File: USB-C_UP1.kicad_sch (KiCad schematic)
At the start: 23 parts, among them J12 USB_C_Receptacle, J13 I2C_HD3SS3220, U26 HD3SS3220IRNHR, U27 TPD4E02B04DQA, U28 TPD4E02B04DQA, U29 TPD4E02B04DQA

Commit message: Added lcsc part number for most of resistors
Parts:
- R93, R94: LCSC Part (none) -> C25764
- R95, R96, R97: LCSC Part (none) -> C105871
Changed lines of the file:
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@@
+			)
+		)
+		(property "LCSC Part" "C105871"
+			(at 81.28 168.91 0)
+			(effects
+				(font
+					(size 1.27 1.27)
+				)
+				(hide yes)
 			)
 		)
@@
 			)
 		)
+		(property "LCSC Part" "C105871"
+			(at 73.66 171.45 0)
+			(effects
+				(font
+					(size 1.27 1.27)
+				)
+				(hide yes)
+			)
+		)
 		(pin "2"
 		)
@@
 			)
 		)
+		(property "LCSC Part" "C25764 "
+			(at 34.29 54.61 0)
+			(effects
+				(font
+					(size 1.27 1.27)
+				)
+				(hide yes)
+			)
+		)
 		(pin "1"
 		)
@@
 			)
 		)
+		(property "LCSC Part" "C25764 "
+			(at 41.91 52.07 0)
+			(effects
+				(font
+					(size 1.27 1.27)
+				)
+				(hide yes)
+			)
+		)
 		(pin "1"
 		)
@@
 			(effects
 				(font
+					(size 1.27 1.27)
+				)
+				(hide yes)
+			)
+		)
+		(property "LCSC Part" "C105871"
+			(at 49.53 66.04 90)
+			(effects
+				(font

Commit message: minor schematic fixes, footprints changes, layout improvements
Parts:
- removed TP11: Out1, TestPoint:TestPoint_Loop_D1.80mm_Drill1.0mm_Beaded, symbol Connector:TestPoint
- removed TP12: Out2, TestPoint:TestPoint_Loop_D1.80mm_Drill1.0mm_Beaded, symbol Connector:TestPoint
- C121: footprint Capacitor_THT:C_Radial_D6.3mm_H11.0mm_P2.50mm -> Capacitor_SMD:C_0805_2012Metric; LCSC Part C109392 -> C141660
- TP10, TP9: footprint TestPoint:TestPoint_Loop_D1.80mm_Drill1.0mm_Beaded -> TestPoint:TestPoint_Pad_D1.0mm
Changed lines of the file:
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@@
 	)
 	(junction
-		(at 60.96 175.26)
-		(diameter 0)
-		(color 0 0 0 0)
-	)
-	(junction
-		(at 52.07 172.72)
-		(diameter 0)
-		(color 0 0 0 0)
-	)
-	(junction
 		(at 233.68 40.64)
 		(diameter 0)
@@
 	(wire
 		(pts
-			(xy 60.96 175.26) (xy 73.66 175.26)
-		)
-		(stroke
-			(width 0)
-			(type default)
-		)
-	)
-	(wire
-		(pts
 			(xy 233.68 66.04) (xy 218.44 66.04)
 		)
@@
 	(wire
 		(pts
-			(xy 30.48 175.26) (xy 60.96 175.26)
+			(xy 30.48 175.26) (xy 73.66 175.26)
 		)
 		(stroke
@@
 	(wire
 		(pts
-			(xy 30.48 172.72) (xy 52.07 172.72)
+			(xy 30.48 172.72) (xy 81.28 172.72)
 		)
 		(stroke
@@
 	(wire
 		(pts
-			(xy 52.07 172.72) (xy 81.28 172.72)
-		)
-		(stroke
-			(width 0)
-			(type default)
-		)
-	)
-	(wire
-		(pts
 			(xy 127 76.2) (xy 140.97 76.2)
 		)
@@
 	)
 	(symbol
-		(lib_id "Connector:TestPoint")
-		(at 52.07 172.72 0)
-		(unit 1)
-		(exclude_from_sim no)
-		(in_bom yes)
-		(on_board yes)
-		(dnp no)
-		(fields_autoplaced yes)
-		(property "Reference" "TP11"
-			(at 54.61 168.1479 0)
-			(effects
-				(font
-					(size 1.27 1.27)
-				)
-				(justify left)
-			)
-		)
-		(property "Value" "Out1"
-			(at 54.61 170.6879 0)
-			(effects
-				(font
-					(size 1.27 1.27)
-				)
-				(justify left)
-			)
-		)
-		(property "Footprint" "TestPoint:TestPoint_Loop_D1.80mm_Drill1.0mm_Beaded"
-			(at 57.15 172.72 0)
-			(effects
-				(font
-					(size 1.27 1.27)
-				)
-				(hide yes)
-			)
-		)
-		(property "Datasheet" "~"
-			(at 57.15 172.72 0)
-			(effects
-				(font
-					(size 1.27 1.27)
-				)
-				(hide yes)
-			)
-		)
-		(property "Description" "test point"
-			(at 52.07 172.72 0)
-			(effects
-				(font
-					(size 1.27 1.27)
-				)
-				(hide yes)
-			)
-		)
-		(pin "1"
-		)
-		(instances
-			(project "USB_hub"
-				(path "/a2586c28-95f1-49e6-9254-37d7a8473e53/c482699f-16ee-4a02-bb28-667e2389d2fc"
-					(reference "TP11")
-					(unit 1)
-				)
-			)
-		)
-	)
-	(symbol
 		(lib_id "2025-07-15_13-22-11:HD3SS3220IRNHR")
 		(at 96.52 66.04 0)
@@
 	)
 	(symbol
-		(lib_id "Connector:TestPoint")
-		(at 60.96 175.26 0)
-		(unit 1)
-		(exclude_from_sim no)
-		(in_bom yes)
-		(on_board yes)
-		(dnp no)
-		(property "Reference" "TP12"
-			(at 63.5 171.196 0)
-			(effects
-				(font
-					(size 1.27 1.27)
-				)
-				(justify left)
-			)
-		)
-		(property "Value" "Out2"
-			(at 63.5 173.736 0)
-			(effects
-				(font
-					(size 1.27 1.27)
-				)
-				(justify left)
-			)
-		)
-		(property "Footprint" "TestPoint:TestPoint_Loop_D1.80mm_Drill1.0mm_Beaded"
-			(at 66.04 175.26 0)
-			(effects
-				(font
-					(size 1.27 1.27)
-				)
-				(hide yes)
-			)
-		)
-		(property "Datasheet" "~"
-			(at 66.04 175.26 0)
-			(effects
-				(font
-					(size 1.27 1.27)
-				)
-				(hide yes)
-			)
-		)
-		(property "Description" "test point"
-			(at 60.96 175.26 0)
-			(effects
-				(font
-					(size 1.27 1.27)
-				)
-				(hide yes)
-			)
-		)
-		(pin "1"
-		)
-		(instances
-			(project "USB_hub"
-				(path "/a2586c28-95f1-49e6-9254-37d7a8473e53/c482699f-16ee-4a02-bb28-667e2389d2fc"
-					(reference "TP12")
-					(unit 1)
-				)
-			)
-		)
-	)
-	(symbol
 		(lib_id "power:VBUS")
 		(at 48.26 41.91 0)
@@
 			)
 		)
-		(property "Footprint" "TestPoint:TestPoint_Loop_D1.80mm_Drill1.0mm_Beaded"
+		(property "Footprint" "TestPoint:TestPoint_Pad_D1.0mm"
 			(at 27.94 162.56 0)
 			(effects
@@
 			)
 		)
-		(property "Footprint" "TestPoint:TestPoint_Loop_D1.80mm_Drill1.0mm_Beaded"
+		(property "Footprint" "TestPoint:TestPoint_Pad_D1.0mm"
 			(at 27.94 154.94 0)
 			(effects
@@
 			)
 		)
-		(property "Footprint" "Capacitor_THT:C_Radial_D6.3mm_H11.0mm_P2.50mm"
+		(property "Footprint" "Capacitor_SMD:C_0805_2012Metric"
 			(at 21.2852 34.29 0)
 			(effects
@@
 			)
 		)
-		(property "LCSC Part" "C109392"
+		(property "LCSC Part" "C141660 "
 			(at 20.32 30.48 0)
 			(effects

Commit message: comments to schematic added, changed a few components
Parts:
- R92: footprint Resistor_SMD:R_0402_1005Metric -> Resistor_SMD:R_1206_3216Metric; Mouser Part No  (none) -> 603-RT1206CRE07900KL
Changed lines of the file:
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@@
 			)
 		)
-		(property "Footprint" "Resistor_SMD:R_0402_1005Metric"
+		(property "Footprint" "Resistor_SMD:R_1206_3216Metric"
 			(at 50.038 45.72 90)
 			(effects
@@
 			(at 48.26 45.72 0)
 			(effects
+				(font
+					(size 1.27 1.27)
+				)
+				(hide yes)
+			)
+		)
+		(property "Mouser Part No " "603-RT1206CRE07900KL "
+			(at 48.26 45.72 0)
+			(effects

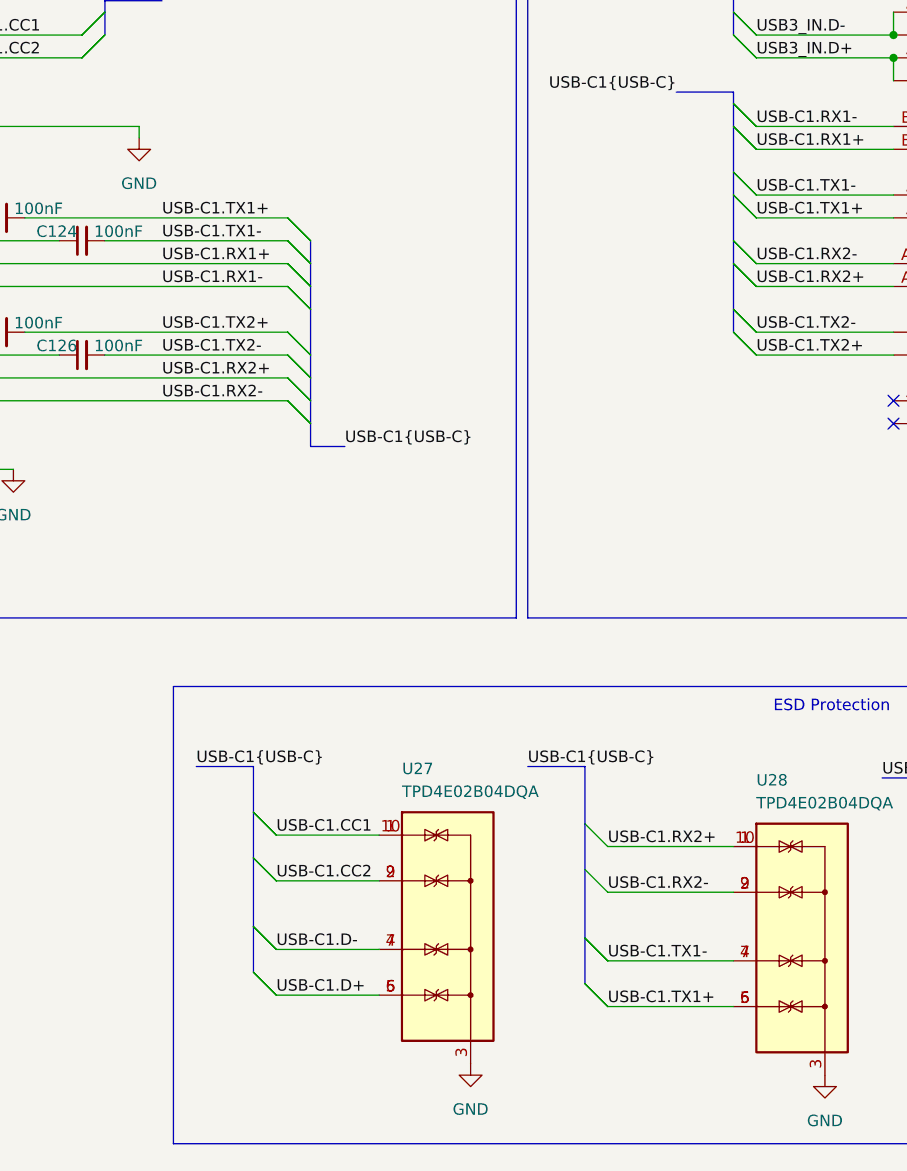
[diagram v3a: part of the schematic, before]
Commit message: Rearrange of the component placement, scheme changes for better routing
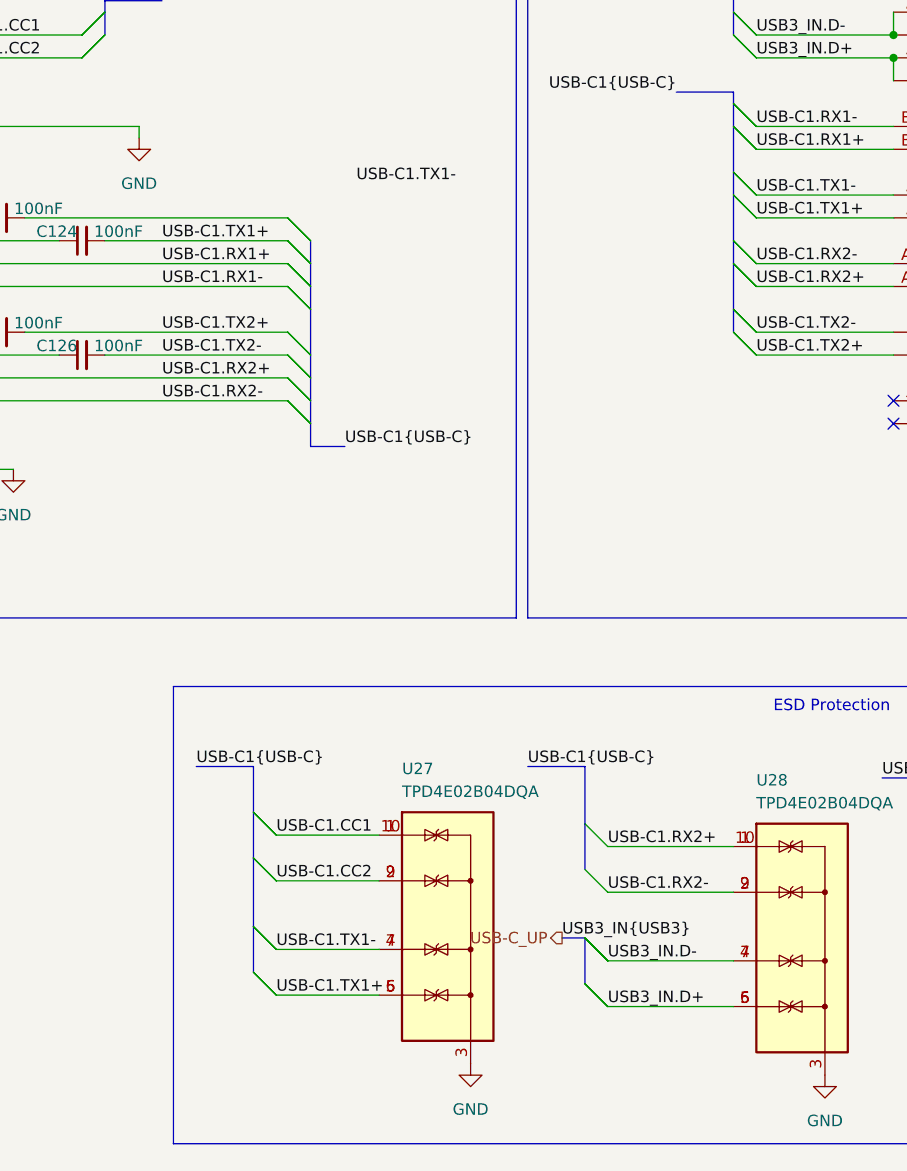
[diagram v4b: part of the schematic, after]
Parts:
- C122, C123, C124, C125, C126: footprint Capacitor_SMD:C_0402_1005Metric -> Capacitor_SMD:C_0201_0603Metric; LCSC Part C5182432 -> C181043
- J13: footprint Connector_PinHeader_1.27mm:PinHeader_1x03_P1.27mm_Vertical -> Connector_PinHeader_1.00mm:PinHeader_1x03_P1.00mm_Vertical
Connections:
- net USB-C1.D+ is gone; now on net USB-C1.TX1+: U27.5 (IO4), U27.6 (NC)
- net USB-C1.D- is gone; now on net USB-C1.TX1-: U27.4 (IO3), U27.7 (NC)
- net USB-C1.TX1+: now also C124.2; no longer C123.2, U28.5 (IO4), U28.6 (NC)
- net USB-C1.TX1-: no longer C124.2, U28.4 (IO3), U28.7 (NC)
- net USB3_IN.D+: now also U28.5 (IO4), U28.6 (NC)
- net USB3_IN.D-: now also U28.4 (IO3), U28.7 (NC)
